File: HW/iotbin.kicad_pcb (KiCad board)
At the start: 2 copper layers, 43 x 35 mm, 15 parts, among them J1 Conn_01x04_Male, J2 Conn_01x02_Male, J3 Conn_01x02_Male, Q1 Q_NMOS_DSG, U1 ESP-12E, U2 HC-SR04, U3 AMS1117-3.3, U4 AMS1117-3.3

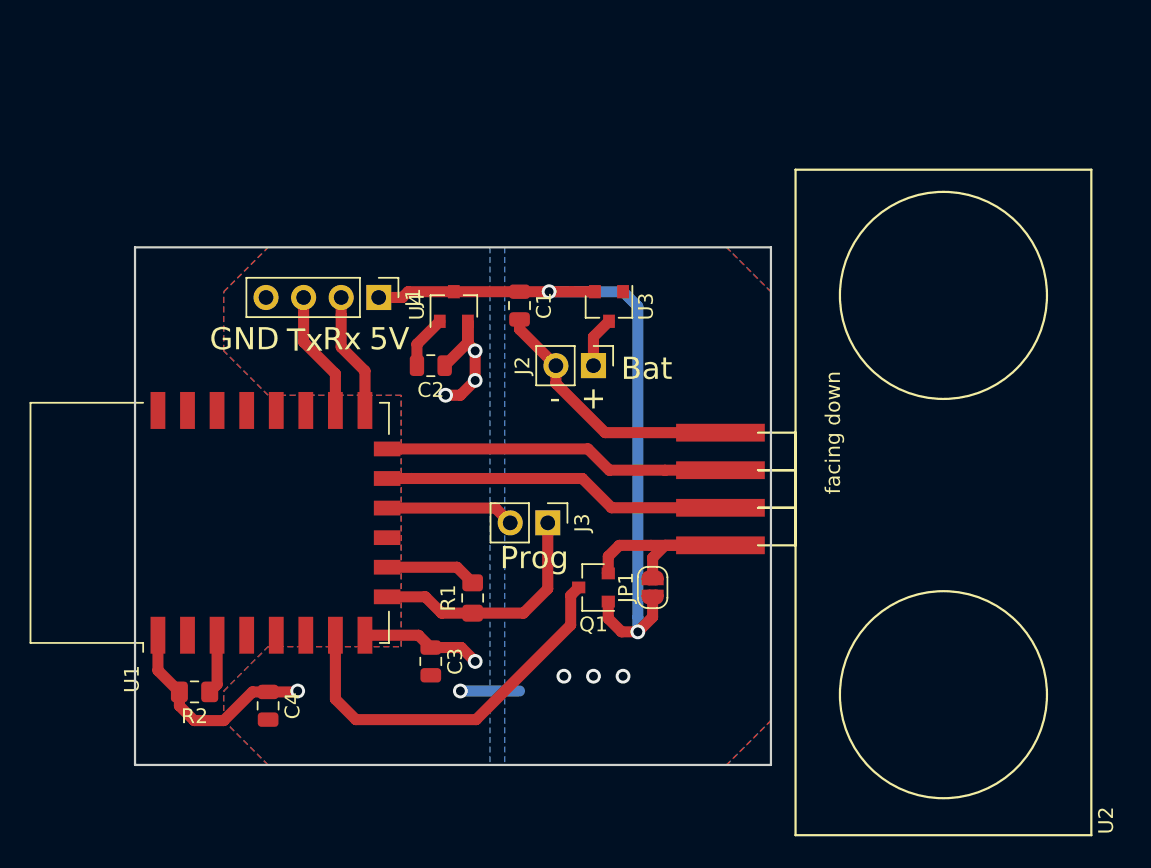
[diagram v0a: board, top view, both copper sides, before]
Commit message: Setting libraries in kicad
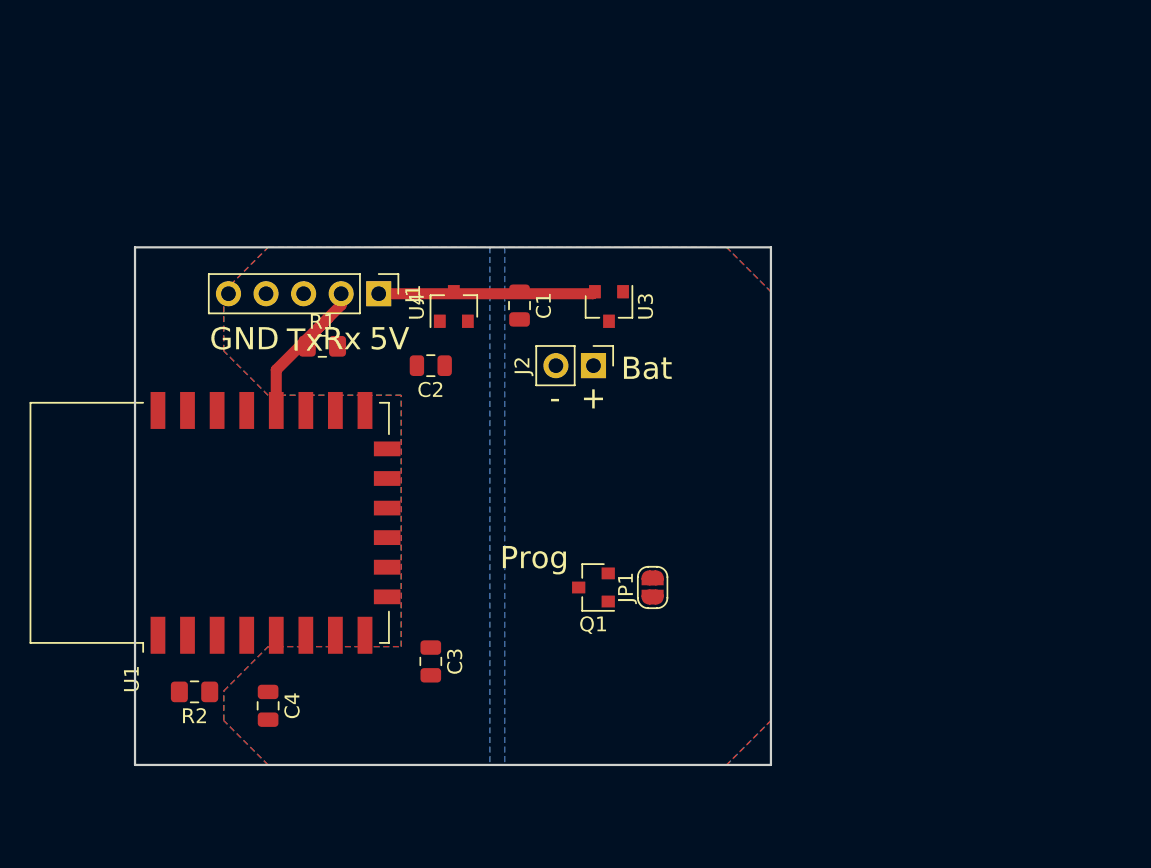
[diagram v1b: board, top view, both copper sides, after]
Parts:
- removed J3: Conn_01x02_Male, Connector_PinHeader_2.54mm:PinHeader_1x02_P2.54mm_Vertical
- removed U2: HC-SR04, HC-SR:HC-SR04_flat_down
- J1: value Conn_01x04_Male -> Conn_01x05_Male; footprint Connector_PinHeader_2.54mm:PinHeader_1x04_P2.54mm_Vertical -> Connector_PinHeader_2.54mm:PinHeader_1x05_P2.54mm_Vertical
- U1: value ESP-12E -> ESP-12F
- moved R1 19.8 mm to (153.7, 75.7), turned to 0 degrees
- moved J1 0.25 mm to (157.5, 72.1)
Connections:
- J1 pad 4: GND -> Net-(J1-Pad4)
- R1 pad 1: GND -> Net-(J1-Pad2)
- R1 pad 2: Net-(R1-Pad2) -> /3V3
- U1 pad 1: /3V3 -> Net-(U1-Pad1)
- U1 pad 10: Net-(R1-Pad2) -> Net-(U1-Pad10)
- U1 pad 15: Net-(J1-Pad2) -> GND
- U1 pad 16: Net-(J1-Pad3) -> GND
- U1 pad 17: Net-(U1-Pad17) -> /3V3
- U1 pad 18: Net-(U1-Pad18) -> Net-(J1-Pad2)
- U1 pad 21: Net-(U1-Pad21) -> Net-(J1-Pad3)
- U1 pad 22: Net-(U1-Pad22) -> Net-(J1-Pad4)
- U1 pad 3: Net-(R2-Pad1) -> Net-(U1-Pad3)
- U1 pad 7: Net-(Q1-Pad3) -> Net-(U1-Pad7)
- U1 pad 9: GND -> Net-(U1-Pad9)
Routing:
- net GND: track 41.9 -> 0.00 mm, vias 4 -> 0
- net /5V: track 49.0 -> 14.7 mm, vias 2 -> 0
- net /3V3: track 33.1 -> 0.00 mm, vias 5 -> 0
- net Net-(Q1-Pad3): track 26.2 -> 0.00 mm
- net Net-(U1-Pad13): track 23.4 -> 0.00 mm
- net Net-(U1-Pad14): track 23.1 -> 0.00 mm
- net /5V_S: track 15.2 -> 0.00 mm
- net Net-(U1-Pad12): track 8.73 -> 0.00 mm
- net Net-(J1-Pad3): track 8.53 -> 0.00 mm
- net Net-(R1-Pad2): track 6.22 -> 0.00 mm
- net Net-(R2-Pad1): track 4.04 -> 0.00 mm
- net Net-(J1-Pad2): track 8.31 -> 12.1 mm
- net /BAT: track 3.43 -> 0.00 mm

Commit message: Tested power modes, added libraries, updated HW
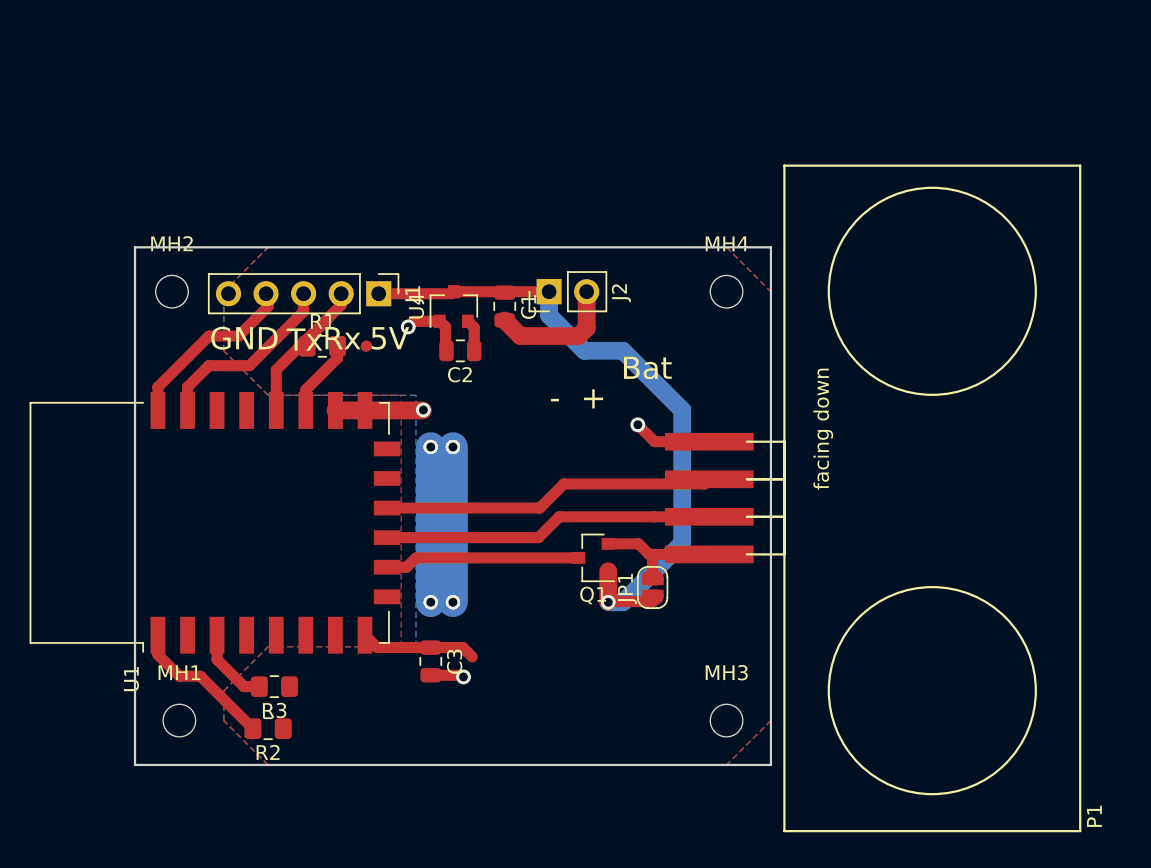
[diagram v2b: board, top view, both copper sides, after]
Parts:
- removed C4: CAP, Capacitor_SMD:C_0805_2012Metric
- removed U3: AMS1117-3.3, Package_TO_SOT_SMD:SOT-23
- added MH1: MountingHole, MountingHole:MountingHole_2.2mm_M2, F.Cu at (144.0, 101.0)
- added MH2: MountingHole, MountingHole:MountingHole_2.2mm_M2, F.Cu at (143.5, 72.0)
- added MH3: MountingHole, MountingHole:MountingHole_2.2mm_M2, F.Cu at (181.0, 101.0)
- added MH4: MountingHole, MountingHole:MountingHole_2.2mm_M2, F.Cu at (181.0, 72.0)
- added P1: hc-sr04, HC-SR:HC-SR04_flat_down, F.Cu at (184.9, 63.5)
- added R3: 10K, Resistor_SMD:R_0805_2012Metric_Pad1.15x1.40mm_HandSolder, F.Cu at (150.4, 98.7)
- R1, R2: value 2K2 -> 10K
- moved J2 5.83 mm to (169.0, 72.0), turned to 90 degrees
- moved R2 5.56 mm to (150.0, 101.5)
- moved C2 2.24 mm to (163.0, 76.0)
- moved Q1 2.00 mm to (172.0, 90.0)
- moved C1 1.00 mm to (166.0, 73.0)
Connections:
- J2 pad 1: /BAT -> /5V
- R2 pad 1: Net-(R2-Pad1) -> /3V3
- R2 pad 2: /3V3 -> Net-(R2-Pad2)
- U1 pad 1: Net-(U1-Pad1) -> Net-(R2-Pad2)
- U1 pad 10: Net-(U1-Pad10) -> Net-(Q1-Pad3)
- U1 pad 11: Net-(U1-Pad11) -> /Trig
- U1 pad 12: Net-(U1-Pad12) -> /Echo
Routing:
- net /3V3: track 0.00 -> 36.4 mm, vias 0 -> 4
- net /5V: track 14.7 -> 45.6 mm, vias 0 -> 1
- net GND: track 0.00 -> 26.7 mm, vias 0 -> 4
- net /Echo: track 0.00 -> 22.6 mm
- net /Trig: track 0.00 -> 22.4 mm
- net Net-(Q1-Pad3): track 0.00 -> 13.2 mm
- net Net-(J1-Pad3): track 0.00 -> 12.7 mm
- net Net-(J1-Pad4): track 0.00 -> 12.2 mm
- net Net-(R2-Pad2): track 0.00 -> 9.82 mm
- net /5V_S: track 0.00 -> 8.57 mm
- net Net-(R3-Pad2): track 0.00 -> 4.93 mm
- added copper zone on F.Cu, net /3V3
- removed copper zone on B.Cu, net /3V3
- removed copper zone on F.Cu, net GND
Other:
- net class power added: clearance 0.6, trace_width 1.2, via_dia 1, via_drill 0.6
- board text removed: "Prog"

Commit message: Finished board+gerber
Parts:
- removed JP1: Jumper, Jumper:SolderJumper-2_P1.3mm_Open_RoundedPad1.0x1.5mm
- removed MH1, MH2, MH3, MH4: MountingHole, MountingHole:MountingHole_2.2mm_M2
- added BT1: Battery, Battery:Battery_AAAx3_no_hole, B.Cu at (160.5, 79.0)
- added R4: 2K, Resistor_SMD:R_0805_2012Metric_Pad1.15x1.40mm_HandSolder, F.Cu at (167.1, 81.5)
- added R5: 0, Resistor_SMD:R_0805_2012Metric_Pad1.15x1.40mm_HandSolder, F.Cu at (178.7, 88.3)
- added R6: 10K, Resistor_SMD:R_0805_2012Metric_Pad1.15x1.40mm_HandSolder, F.Cu at (157.6, 77.1)
- J2: footprint Connector_PinHeader_2.54mm:PinHeader_1x02_P2.54mm_Vertical -> Connector_PinHeader_2.00mm:PinHeader_1x02_P2.00mm_Vertical
- R2: value 10K -> 1K
- moved J2 30.2 mm to (155.8, 99.2), turned to 270 degrees
- moved R2 28.2 mm to (169.9, 81.5), turned to 270 degrees
- moved P1 9.14 mm to (185.4, 54.4)
- moved Q1 4.00 mm to (174.4, 86.8)
- moved R3 1.60 mm to (150.4, 100.3)
- moved C3 1.39 mm to (162.1, 96.2), turned to 0 degrees
- moved R1 0.98 mm to (154.2, 74.9)
- moved C2 0.85 mm to (163.8, 76.0)
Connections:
- J2 pad 1: /5V -> Net-(J2-Pad1)
- J2 pad 2: GND -> Net-(J2-Pad2)
- R2 pad 1: /3V3 -> /Echo
- U1 pad 1: Net-(R2-Pad2) -> /RST
- U1 pad 12: /Echo -> Net-(R2-Pad2)
- U1 pad 16: GND -> Net-(R6-Pad1)
- U1 pad 4: Net-(U1-Pad4) -> /RST
- U1 pad 6: Net-(U1-Pad6) -> Net-(J2-Pad2)
- U1 pad 7: Net-(U1-Pad7) -> Net-(J2-Pad1)
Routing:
- net /RST: track 0.00 -> 16.8 mm
- net /5V: track 45.6 -> 59.4 mm, vias 1 -> 2
- net /Echo: track 22.6 -> 12.4 mm
- net GND: track 26.7 -> 33.0 mm, vias 4 -> 5
- net /5V_S: track 8.57 -> 14.5 mm
- net /3V3: track 36.4 -> 41.4 mm
- net Net-(J2-Pad1): track 0.00 -> 4.44 mm
- net /Trig: track 22.4 -> 26.6 mm
- net Net-(R6-Pad1): track 0.00 -> 4.11 mm
- net Net-(J2-Pad2): track 0.00 -> 4.03 mm
- net Net-(R3-Pad2): track 4.93 -> 8.81 mm
- net Net-(R2-Pad2): track 9.82 -> 13.6 mm
- net Net-(Q1-Pad3): track 13.2 -> 16.9 mm
- net Net-(J1-Pad2): track 12.1 -> 10.0 mm
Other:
- rule trace_min: 0.2 -> 0.25
- rule via_min_size: 0.4 -> 0.5

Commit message: Sent gerbers 1.2
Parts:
- removed Q1: Q_NMOS_DSG, Package_TO_SOT_SMD:SOT-23
- added R7: 1M, Resistor_SMD:R_0805_2012Metric_Pad1.15x1.40mm_HandSolder, F.Cu at (175.8, 91.7)
- added R8: 1K, Resistor_SMD:R_0805_2012Metric_Pad1.15x1.40mm_HandSolder, F.Cu at (165.9, 93.5)
- added U2: FDV302P, Package_TO_SOT_SMD:SOT-23, F.Cu at (173.2, 87.4)
- added U3: FDV303N, Package_TO_SOT_SMD:SOT-23, F.Cu at (170.2, 92.5)
- U4: value AMS1117-3.3 -> AP2204RB-3.3; footprint Package_TO_SOT_SMD:SOT-23 -> Package_TO_SOT_SMD:SOT-223-3_TabPin2
- moved C1 7.17 mm to (173.0, 74.7)
- moved U4 6.14 mm to (167.6, 76.5), turned to 270 degrees
- moved J2 4.67 mm to (151.1, 99.1), turned to 90 degrees
- moved R4 4.39 mm to (165.4, 85.6)
- moved R2 2.61 mm to (168.7, 83.8), turned to 225 degrees
- moved C2 2.05 mm to (161.8, 75.9), turned to 225 degrees
- moved R3 1.78 mm to (151.6, 101.6)
- moved C3 0.19 mm to (162.1, 96.0)
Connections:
- BT1 pad 1: /5V -> /BAT
- C1 pad 1: /5V -> /BAT
- J1 pad 1: /5V -> /BAT
- R5 pad 2: /5V -> /BAT
- U1 pad 5: Net-(U1-Pad5) -> Net-(J2-Pad1)
- U1 pad 7: Net-(J2-Pad1) -> /ON
- U4 pad 1: GND -> /BAT
- U4 pad 2: /3V3 -> GND
- U4 pad 3: /5V -> /3V3
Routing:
- net /BAT: track 0.00 -> 68.8 mm, vias 0 -> 3
- net /5V: track 59.4 -> 0.00 mm, vias 2 -> 0
- net /ON: track 0.00 -> 19.6 mm
- net Net-(U1-Pad10): track 16.9 -> 0.00 mm
- net GND: track 33.0 -> 44.3 mm
- net Net-(R7-Pad1): track 0.00 -> 7.78 mm
- net /5V_S: track 14.5 -> 17.8 mm
- net Net-(R2-Pad2): track 13.6 -> 10.7 mm
- net Net-(R3-Pad2): track 8.81 -> 10.6 mm
- net /Echo: track 12.4 -> 14.1 mm
- net /3V3: track 41.4 -> 43.0 mm, vias 4 -> 3
- net Net-(J1-Pad4): track 12.2 -> 12.8 mm
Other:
- board text removed: "5V"
- board text removed: "Bat"
- board text removed: "GND"
- board text removed: "Rx"
- board text removed: "Tx"
